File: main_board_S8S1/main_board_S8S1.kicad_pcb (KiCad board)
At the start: 2 copper layers, 114.3 x 86.4 mm, 47 parts

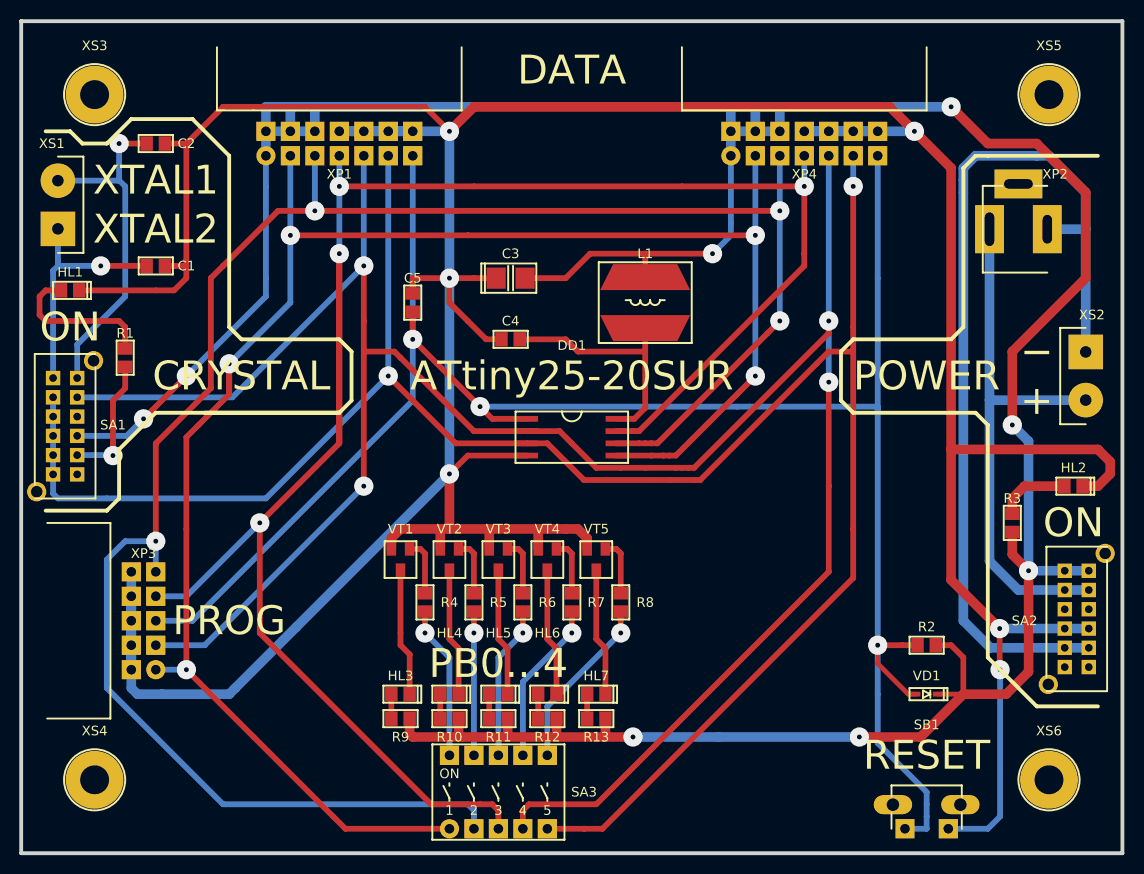
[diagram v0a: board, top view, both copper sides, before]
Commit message: Заменён футпринт контроллера
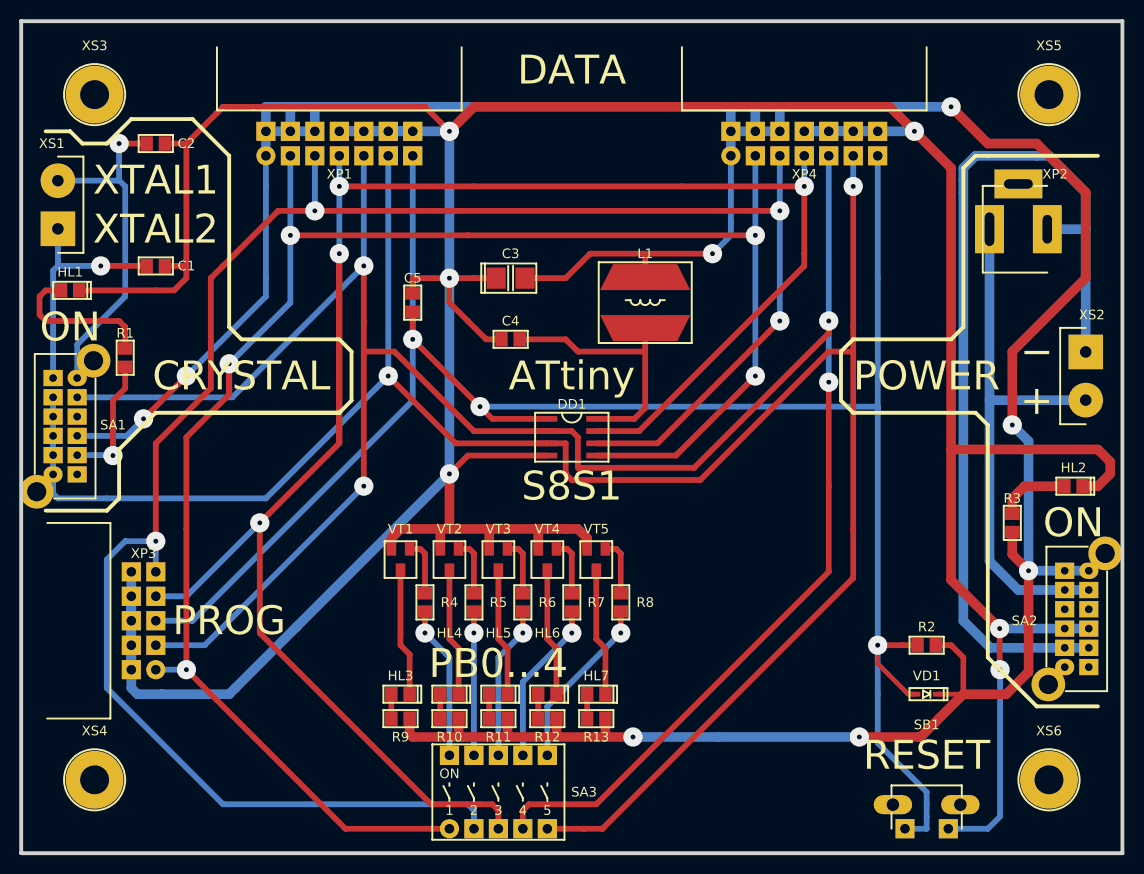
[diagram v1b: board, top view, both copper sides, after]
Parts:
- DD1: footprint KCL:SO-08W -> KCL:SO-08
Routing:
- net GND: track 422.0 -> 424.0 mm
- net /VCC: track 25.3 -> 27.3 mm
- net /PB5: track 207.1 -> 209.1 mm
- net /PB2: track 207.2 -> 209.2 mm
- net /PB1: track 204.4 -> 206.4 mm
- net /PB0: track 187.3 -> 189.3 mm
- net /PB4: track 217.7 -> 219.6 mm
- net /PB3: track 245.5 -> 247.4 mm
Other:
- net class Default: trace_width 1 -> 0.6
- board text added: "ATtiny"
- board text added: "S8S1"
- board text removed: "ATtiny25-20SUR"

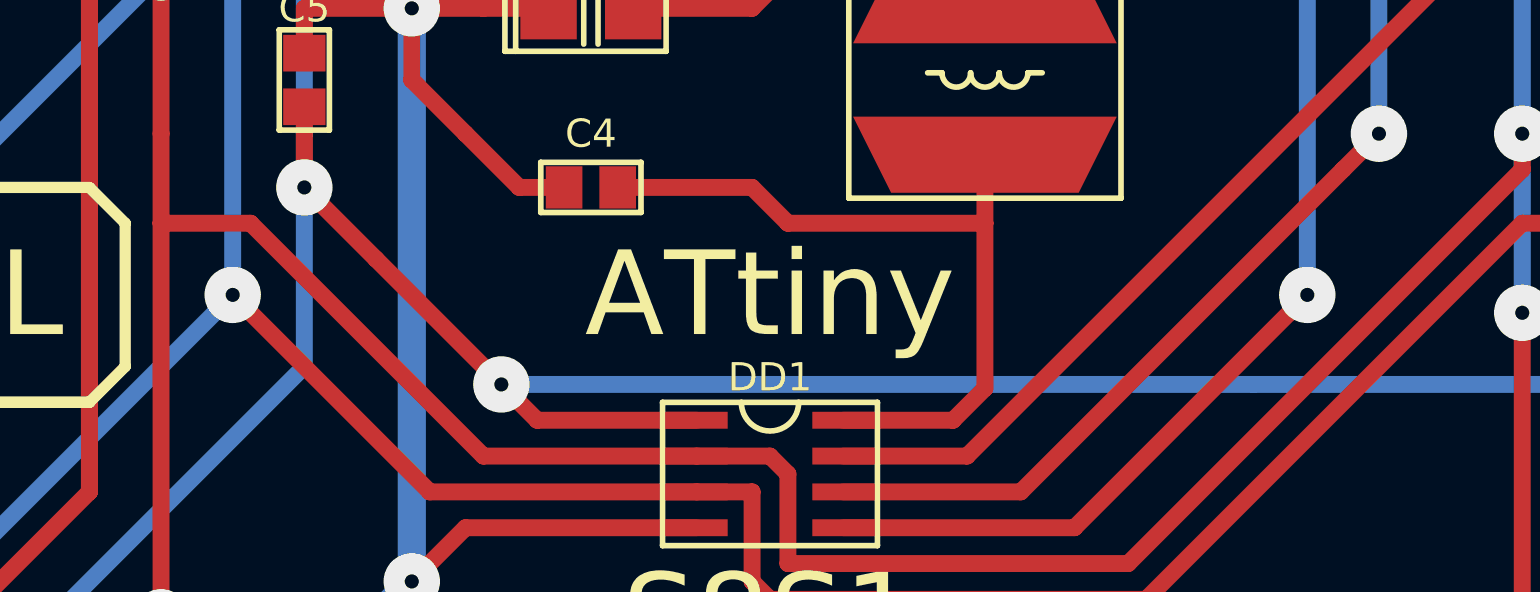
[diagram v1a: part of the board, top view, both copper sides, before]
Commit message: Заменён символ контроллера
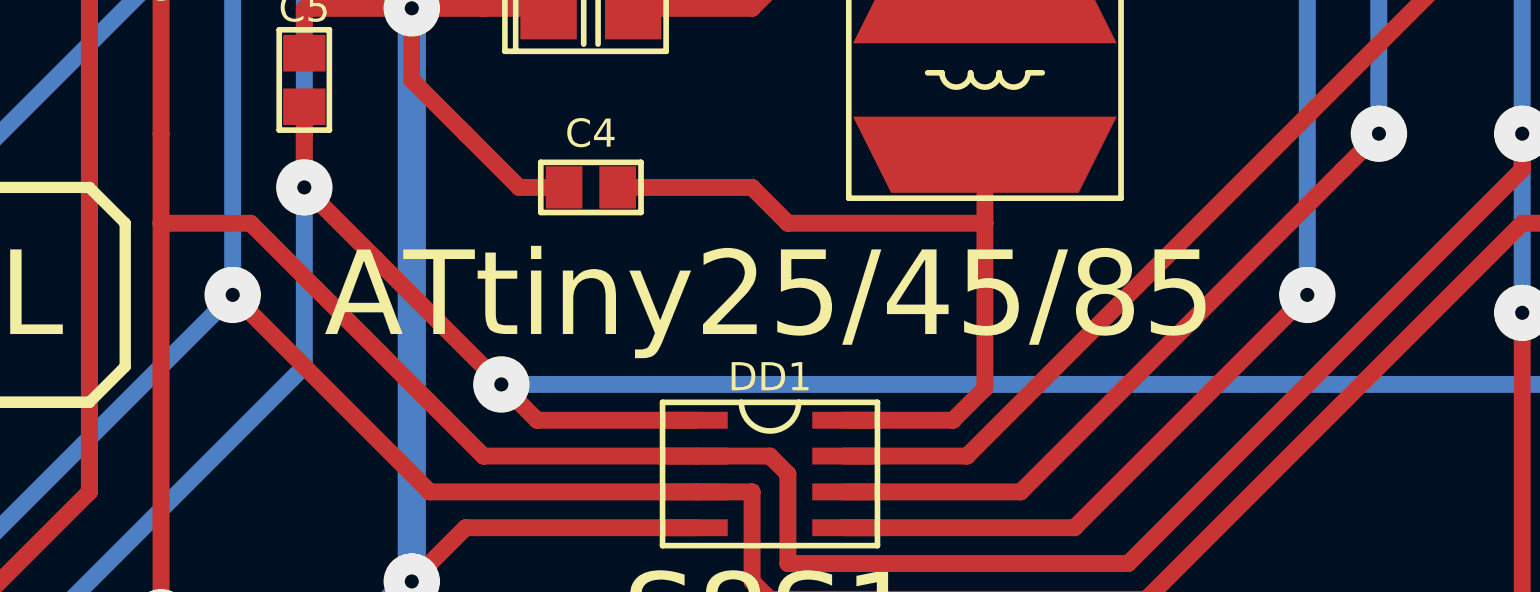
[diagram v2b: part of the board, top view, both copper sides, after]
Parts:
- DD1: value IC_MCU_ATtiny25-20SUR -> IC_MCU_AVR_TINY_25-45-85_S8S1
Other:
- board text added: "ATtiny25/45/85"
- board text removed: "ATtiny"
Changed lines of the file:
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@@
       (effects (font (size 1 1) (thickness 0.2)))
     )
-    (fp_text value IC_MCU_ATtiny25-20SUR (at 0 -4.699) (layer F.Fab) hide
+    (fp_text value IC_MCU_AVR_TINY_25-45-85_S8S1 (at 0 -4.699) (layer F.Fab) hide
       (effects (font (size 1 1) (thickness 0.2)))
     )
@@
   (gr_line (start 205.74 60.96) (end 205.74 147.32) (angle 90) (layer Edge.Cuts) (width 0.4))
   (gr_line (start 91.44 60.96) (end 205.74 60.96) (angle 90) (layer Edge.Cuts) (width 0.4))
-  (gr_text ATtiny (at 148.59 97.79) (layer F.SilkS)
+  (gr_text ATtiny25/45/85 (at 148.59 97.79) (layer F.SilkS)
     (effects (font (size 3 3) (thickness 0.6)))
   )

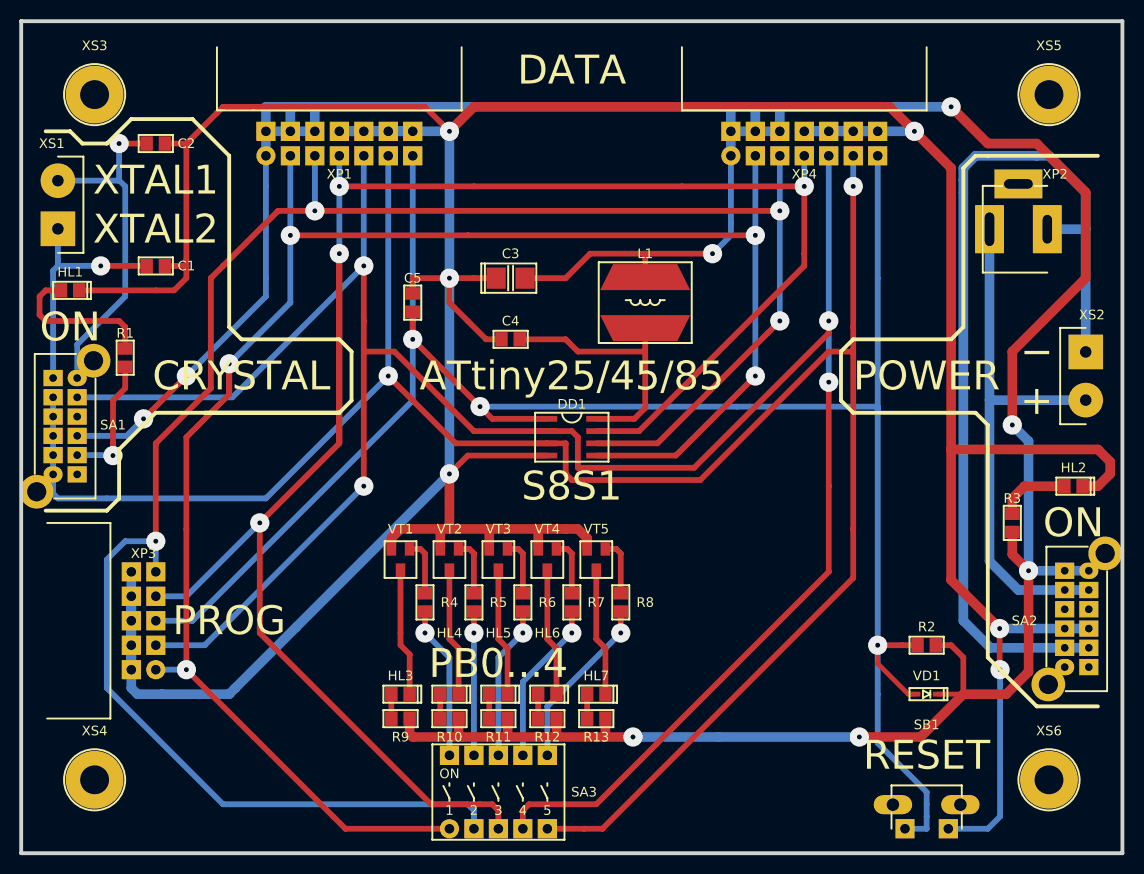
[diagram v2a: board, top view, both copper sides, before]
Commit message: Обновлены футпринты ключей
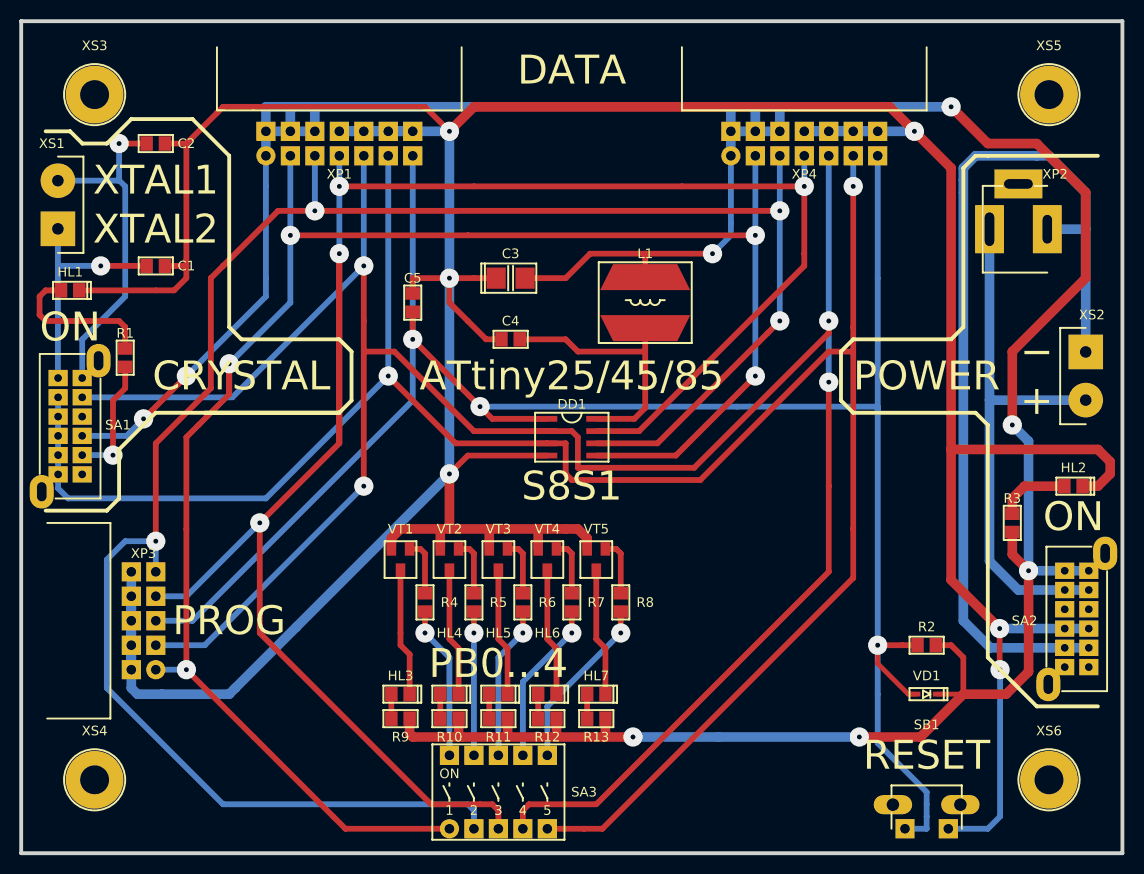
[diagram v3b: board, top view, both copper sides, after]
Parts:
- moved SA1 0.52 mm to (96.5, 103.0)
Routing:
- net /PB4: track 219.6 -> 218.7 mm
- net Net-(R1-Pad1): track 13.5 -> 12.9 mm
- net /PB3: track 247.4 -> 246.9 mm
- net +5V: track 344.5 -> 343.9 mm
